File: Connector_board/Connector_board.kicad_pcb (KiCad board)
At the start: 2 copper layers, 54.2 x 20 mm, 7 parts, among them J1 SM03B-SRSS-TB, J2 USB_B_Micro, J3 Conn_02x07_Counter_Clockwise, J4 Conn_02x07_Odd_Even, J5 Conn_02x07_Counter_Clockwise

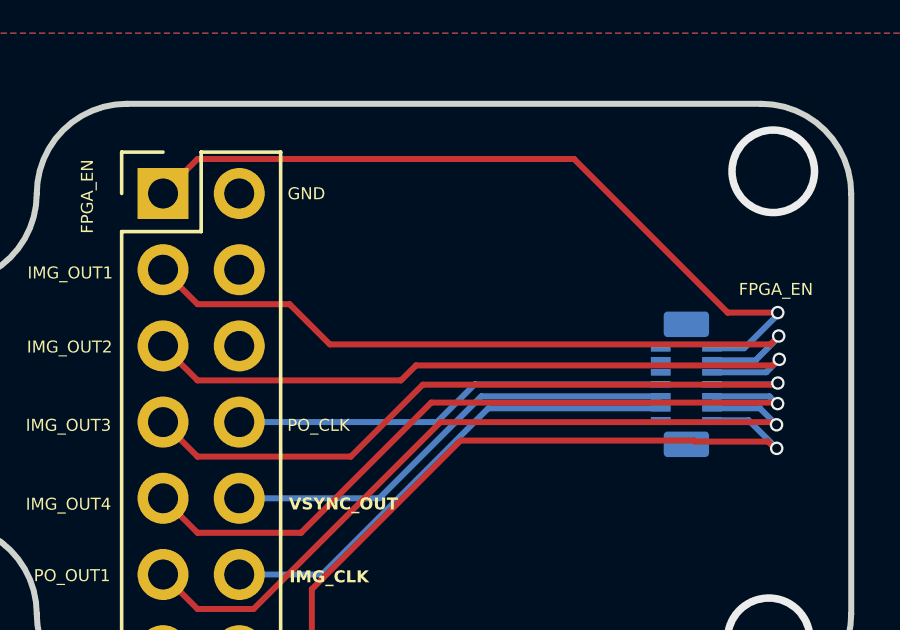
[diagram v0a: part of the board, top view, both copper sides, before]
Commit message: GPIO_1 added
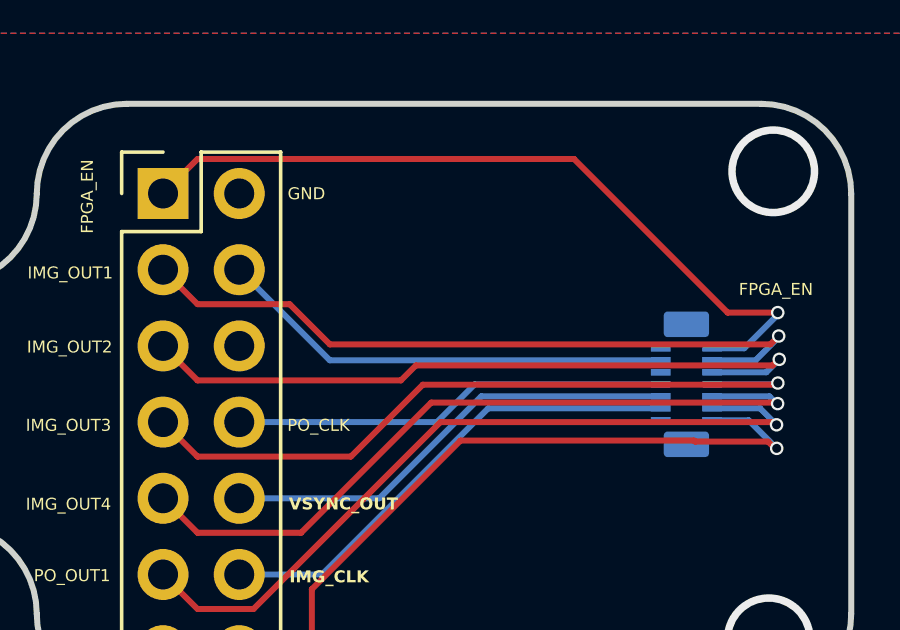
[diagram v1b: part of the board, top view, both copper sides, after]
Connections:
- J4 pad 11: /POSITION_OUT_1 -> /FPGA_CTRL
- J4 pad 4: unconnected-(J4-Pin_4-Pad4) -> /POSITION_OUT_1
- J5 pad 12: unconnected-(J5-Pin_12-Pad12) -> /POSITION_OUT_1
- J5 pad 3: /POSITION_OUT_1 -> /FPGA_CTRL
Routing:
- net /FPGA_CTRL: track 0.00 -> 25.9 mm, vias 0 -> 1
- net /POSITION_OUT_1: track 25.9 -> 15.3 mm, vias 1 -> 0
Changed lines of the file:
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@@
 			(layers "*.Cu" "*.Mask")
 			(remove_unused_layers no)
-			(net "unconnected-(J4-Pin_4-Pad4)")
+			(net "/POSITION_OUT_1")
 			(pinfunction "Pin_4_4")
-			(pintype "passive+no_connect")
+			(pintype "passive")
 		)
 		(pad "5" thru_hole circle
@@
 			(layers "*.Cu" "*.Mask")
 			(remove_unused_layers no)
-			(net "/POSITION_OUT_1")
+			(net "/FPGA_CTRL")
 			(pinfunction "Pin_11_11")
 			(pintype "passive")
@@
 			(size 0.22 0.66)
 			(layers "B.Cu" "B.Mask" "B.Paste")
-			(net "/POSITION_OUT_1")
+			(net "/FPGA_CTRL")
 			(pinfunction "Pin_3_3")
 			(pintype "passive")
@@
 			(size 0.22 0.66)
 			(layers "B.Cu" "B.Mask" "B.Paste")
-			(net "unconnected-(J5-Pin_12-Pad12)")
+			(net "/POSITION_OUT_1")
 			(pinfunction "Pin_12_12")
-			(pintype "passive+no_connect")
+			(pintype "passive")
 		)
 		(pad "13" smd rect
@@
 	)
 	(segment
-		(start 47.66 49.54)
-		(end 46.51 48.39)
-		(width 0.2)
-		(layer "F.Cu")
+		(start 52.07 41.25)
+		(end 49.05 38.23)
+		(width 0.2)
+		(layer "B.Cu")
 		(net "/POSITION_OUT_1")
 	)
 	(segment
-		(start 66.854856 43.31)
-		(end 55.756346 43.31)
-		(width 0.2)
-		(layer "F.Cu")
-		(net "/POSITION_OUT_1")
-	)
-	(segment
-		(start 55.756346 43.31)
-		(end 49.526346 49.54)
-		(width 0.2)
-		(layer "F.Cu")
-		(net "/POSITION_OUT_1")
-	)
-	(segment
-		(start 66.96 43.4)
-		(end 66.944856 43.4)
-		(width 0.2)
-		(layer "F.Cu")
-		(net "/POSITION_OUT_1")
-	)
-	(segment
-		(start 49.526346 49.54)
-		(end 47.66 49.54)
-		(width 0.2)
-		(layer "F.Cu")
-		(net "/POSITION_OUT_1")
-	)
-	(segment
-		(start 66.944856 43.4)
-		(end 66.854856 43.31)
-		(width 0.2)
-		(layer "F.Cu")
-		(net "/POSITION_OUT_1")
-	)
-	(via
-		(at 66.96 43.4)
-		(size 0.45)
-		(drill 0.3)
-		(layers "F.Cu" "B.Cu")
-		(net "/POSITION_OUT_1")
-	)
-	(segment
-		(start 66.41 42.85)
-		(end 64.81 42.85)
-		(width 0.2)
-		(layer "B.Cu")
-		(net "/POSITION_OUT_1")
-	)
-	(segment
-		(start 66.96 43.4)
-		(end 66.41 42.85)
+		(start 63.1 41.25)
+		(end 52.07 41.25)
 		(width 0.2)
 		(layer "B.Cu")
@@
 		(net "/USB_D1+")
 	)
+	(segment
+		(start 47.66 49.54)
+		(end 46.51 48.39)
+		(width 0.2)
+		(layer "F.Cu")
+		(net "/FPGA_CTRL")
+	)
+	(segment
+		(start 66.854856 43.31)
+		(end 55.756346 43.31)
+		(width 0.2)
+		(layer "F.Cu")
+		(net "/FPGA_CTRL")
+	)
+	(segment
+		(start 55.756346 43.31)
+		(end 49.526346 49.54)
+		(width 0.2)
+		(layer "F.Cu")
+		(net "/FPGA_CTRL")
+	)
+	(segment
+		(start 66.96 43.4)
+		(end 66.944856 43.4)
+		(width 0.2)
+		(layer "F.Cu")
+		(net "/FPGA_CTRL")
+	)
+	(segment
+		(start 49.526346 49.54)
+		(end 47.66 49.54)
+		(width 0.2)
+		(layer "F.Cu")
+		(net "/FPGA_CTRL")
+	)
+	(segment
+		(start 66.944856 43.4)
+		(end 66.854856 43.31)
+		(width 0.2)
+		(layer "F.Cu")
+		(net "/FPGA_CTRL")
+	)
+	(via
+		(at 66.96 43.4)
+		(size 0.45)
+		(drill 0.3)
+		(layers "F.Cu" "B.Cu")
+		(net "/FPGA_CTRL")
+	)
+	(segment
+		(start 66.41 42.85)
+		(end 64.81 42.85)
+		(width 0.2)
+		(layer "B.Cu")
+		(net "/FPGA_CTRL")
+	)
+	(segment
+		(start 66.96 43.4)
+		(end 66.41 42.85)
+		(width 0.2)
+		(layer "B.Cu")
+		(net "/FPGA_CTRL")
+	)
 	(zone

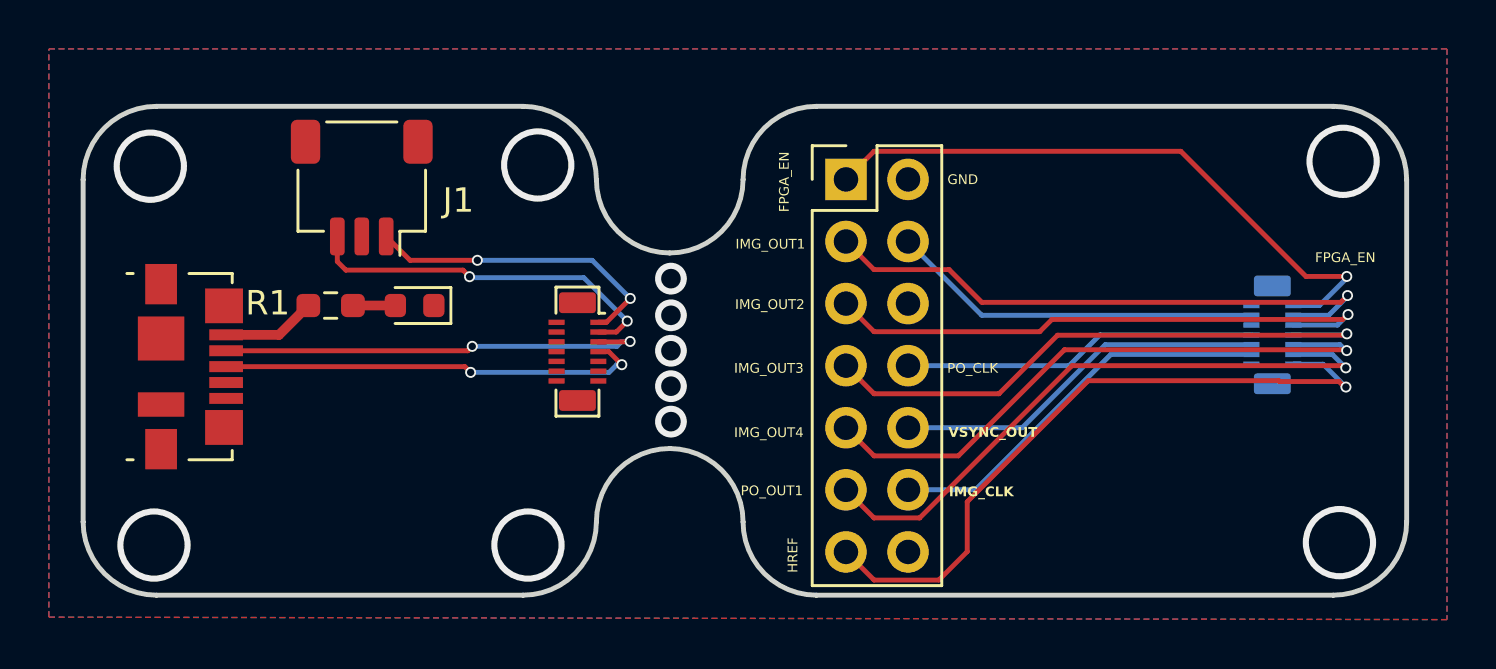
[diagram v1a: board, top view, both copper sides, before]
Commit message: connector board pin order updated
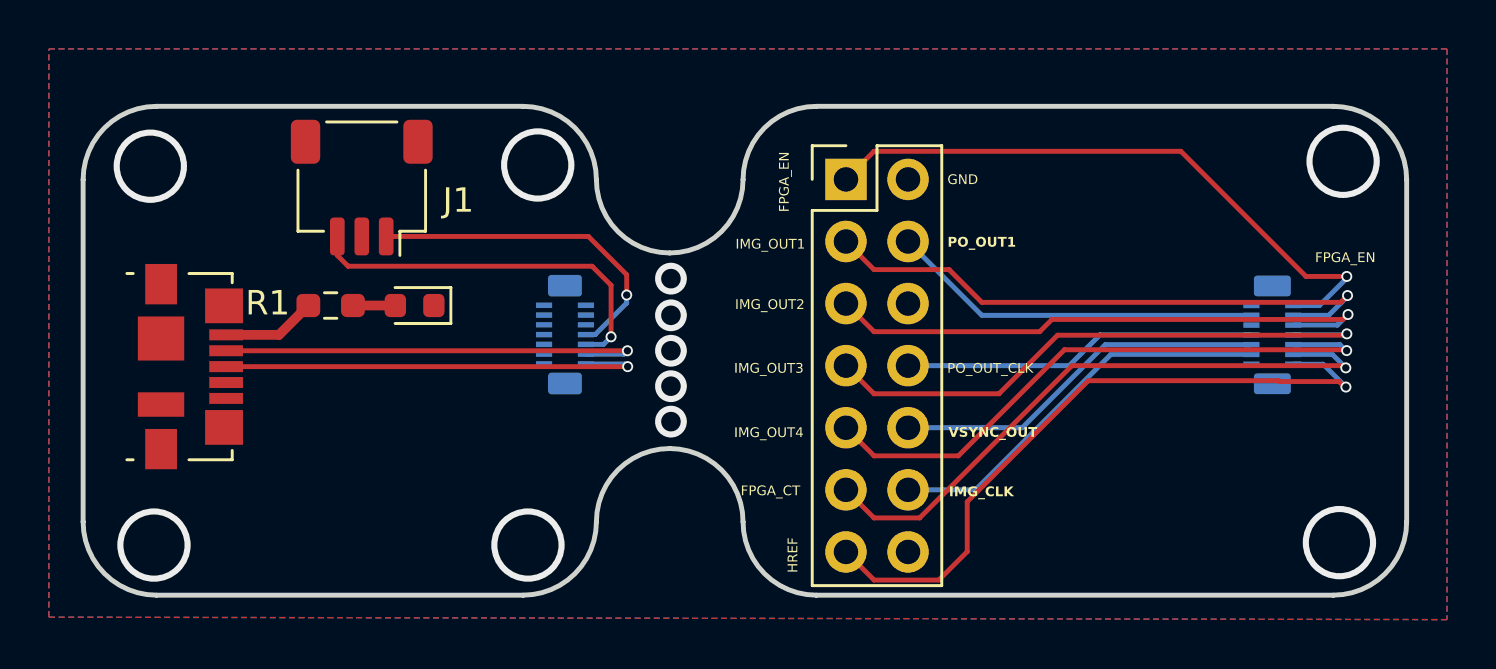
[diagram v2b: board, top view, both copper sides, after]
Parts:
- J3: moved to B.Cu
- moved J3 0.86 mm to (35.0, 42.0), turned to 90 degrees
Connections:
- J3 pad 1: /SWD_1 -> /USB_D1+
- J3 pad 3: /SWCLK_1 -> /USB_D1-
- J3 pad 5: /USB_D1- -> /SWCLK_1
- J3 pad 7: /USB_D1+ -> /SWD_1
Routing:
- net /SWD_1: track 13.2 -> 14.3 mm, vias 2 -> 1
- net /USB_D1+: track 17.6 -> 18.2 mm, vias 2 -> 1
- net /SWCLK_1: track 15.2 -> 15.7 mm, vias 2 -> 1
- net /USB_D1-: track 18.0 -> 18.2 mm, vias 2 -> 1
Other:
- board text added: "FPGA_CT"
- board text added: "PO_OUT_CLK"
- board text removed: "PO_CLK"

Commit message: new connector footprint updated
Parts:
- removed J4: Conn_02x07_Odd_Even, Connector_PinHeader_2.54mm:PinHeader_2x07_P2.54mm_Vertical
- added J6: Conn_02x06_Top_Bottom, 5035521222:CON_5035521222, B.Cu at (34.8, 42.2)
- J3: value Conn_02x07_Counter_Clockwise -> Conn_02x06_Odd_Even; footprint Connector_Molex:Molex_SlimStack_502430-1410_2x07_P0.40mm_Vertical -> Connector_PinHeader_2.54mm:PinHeader_2x06_P2.54mm_Vertical; moved to F.Cu
- J5: value Conn_02x07_Counter_Clockwise -> Conn_02x06_Top_Bottom; footprint Connector_Molex:Molex_SlimStack_502430-1410_2x07_P0.40mm_Vertical -> 5035521222:CON_5035521222
- moved J3 14.0 mm to (47.9, 36.5), turned to 0 degrees
- moved J5 0.91 mm to (64.2, 42.9)
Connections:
- J3 pad 1: /USB_D1+ -> GND
- J3 pad 10: unconnected-(J3-Pin_10-Pad10) -> /IMAGE_OUT_4
- J3 pad 11: unconnected-(J3-Pin_11-Pad11) -> /HREF_OUT
- J3 pad 12: unconnected-(J3-Pin_12-Pad12) -> /FPGA_CTRL
- J3 pad 2: unconnected-(J3-Pin_2-Pad2) -> /FPGA_EN
- J3 pad 3: /USB_D1- -> /POSITION_OUT_1
- J3 pad 4: unconnected-(J3-Pin_4-Pad4) -> /IMAGE_OUT_1
- J3 pad 5: /SWCLK_1 -> /POSITION_OUT_CLK
- J3 pad 6: unconnected-(J3-Pin_6-Pad6) -> /IMAGE_OUT_2
- J3 pad 7: /SWD_1 -> /VSYNC_OUT
- J3 pad 8: unconnected-(J3-Pin_8-Pad8) -> /IMAGE_OUT_3
- J3 pad 9: unconnected-(J3-Pin_9-Pad9) -> /IMAGE_CLK
- J5 pad 1: /HREF_OUT -> /FPGA_CTRL
- J5 pad 10: unconnected-(J5-Pin_10-Pad10) -> /POSITION_OUT_CLK
- J5 pad 11: /IMAGE_OUT_1 -> /POSITION_OUT_1
- J5 pad 12: /POSITION_OUT_1 -> GND
- J5 pad 2: unconnected-(J5-Pin_2-Pad2) -> /IMAGE_OUT_4
- J5 pad 3: /FPGA_CTRL -> /IMAGE_OUT_3
- J5 pad 4: /IMAGE_CLK -> /IMAGE_OUT_2
- J5 pad 5: /IMAGE_OUT_4 -> /IMAGE_OUT_1
- J5 pad 6: /VSYNC_OUT -> /FPGA_EN
- J5 pad 7: /IMAGE_OUT_3 -> /HREF_OUT
- J5 pad 8: /POSITION_OUT_CLK -> /IMAGE_CLK
- J5 pad 9: /IMAGE_OUT_2 -> /VSYNC_OUT
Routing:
- net /HREF_OUT: track 28.2 -> 18.4 mm, vias 1 -> 0
- net /FPGA_EN: track 25.8 -> 21.5 mm
- net /IMAGE_OUT_3: track 24.2 -> 20.4 mm
- net /FPGA_CTRL: track 25.9 -> 22.2 mm
- net /IMAGE_OUT_4: track 24.9 -> 21.3 mm
- net /IMAGE_OUT_2: track 23.7 -> 20.5 mm
- net GND: track 0.00 -> 3.04 mm, vias 11 -> 13
- net /IMAGE_OUT_1: track 24.2 -> 21.4 mm
- net /POSITION_OUT_1: track 15.3 -> 16.6 mm
- net /VSYNC_OUT: track 15.5 -> 16.6 mm
- net /IMAGE_CLK: track 16.3 -> 17.5 mm
- net /POSITION_OUT_CLK: track 14.6 -> 15.7 mm
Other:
- board text added: "FPGA_CTRL"
- board text added: "HREF_OUT"
- board text added: "PO_OUT_1"
- board text removed: "FPGA_CT"
- board text removed: "HREF"
- board text removed: "PO_OUT1"

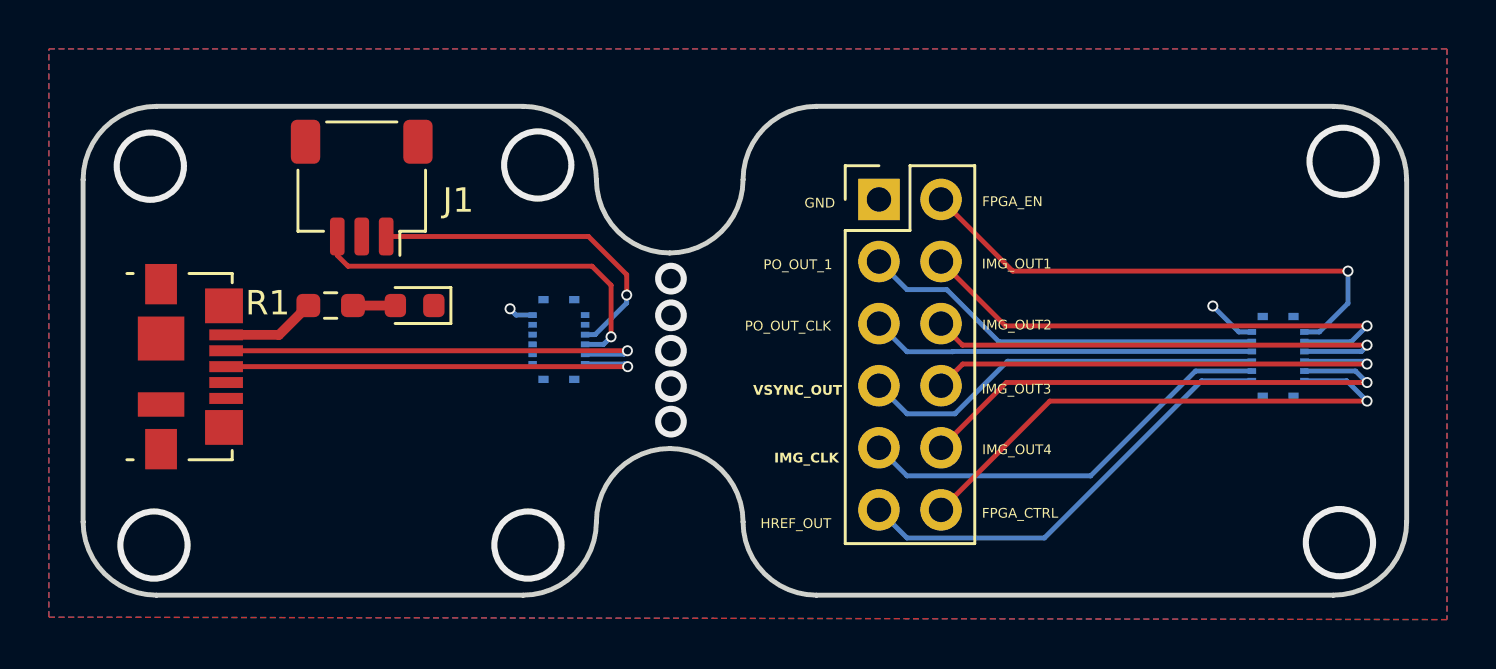
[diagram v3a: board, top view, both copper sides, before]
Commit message: connector footprint swapped
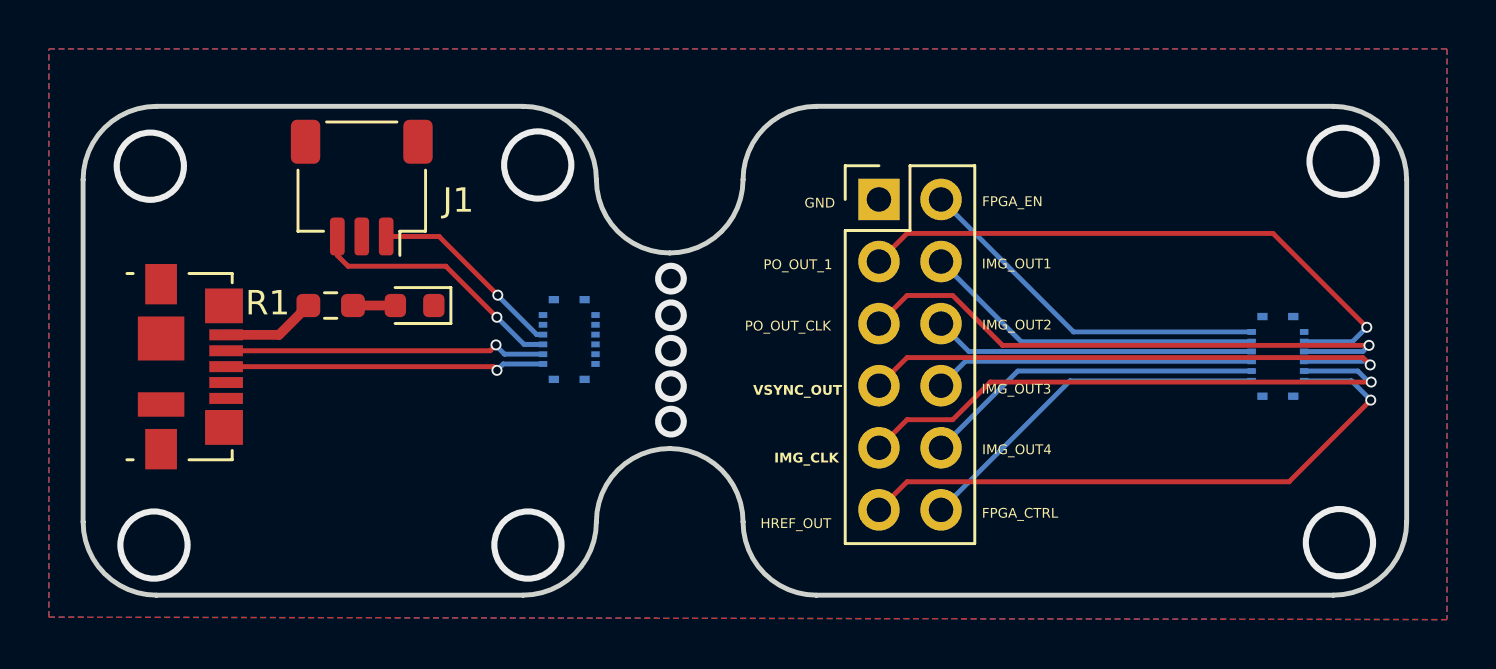
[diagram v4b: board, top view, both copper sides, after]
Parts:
- moved J6 0.42 mm to (35.2, 42.2)
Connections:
- J5 pad 1: /FPGA_CTRL -> /HREF_OUT
- J5 pad 10: /POSITION_OUT_CLK -> /IMAGE_OUT_2
- J5 pad 11: /POSITION_OUT_1 -> /IMAGE_OUT_1
- J5 pad 12: GND -> /FPGA_EN
- J5 pad 2: /IMAGE_OUT_4 -> /IMAGE_CLK
- J5 pad 3: /IMAGE_OUT_3 -> /VSYNC_OUT
- J5 pad 4: /IMAGE_OUT_2 -> /POSITION_OUT_CLK
- J5 pad 5: /IMAGE_OUT_1 -> /POSITION_OUT_1
- J5 pad 6: /FPGA_EN -> GND
- J5 pad 7: /HREF_OUT -> /FPGA_CTRL
- J5 pad 8: /IMAGE_CLK -> /IMAGE_OUT_4
- J5 pad 9: /VSYNC_OUT -> /IMAGE_OUT_3
- J6 pad 1: /USB_D1+ -> unconnected-(J6-Pin_1-Pad1)
- J6 pad 10: unconnected-(J6-Pin_10-Pad10) -> /SWD_1
- J6 pad 12: GND -> unconnected-(J6-Pin_12-Pad12)
- J6 pad 2: /USB_D1- -> unconnected-(J6-Pin_2-Pad2)
- J6 pad 3: /SWCLK_1 -> unconnected-(J6-Pin_3-Pad3)
- J6 pad 4: /SWD_1 -> unconnected-(J6-Pin_4-Pad4)
- J6 pad 6: unconnected-(J6-Pin_6-Pad6) -> GND
- J6 pad 7: unconnected-(J6-Pin_7-Pad7) -> /USB_D1+
- J6 pad 8: unconnected-(J6-Pin_8-Pad8) -> /USB_D1-
- J6 pad 9: unconnected-(J6-Pin_9-Pad9) -> /SWCLK_1
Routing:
- net /POSITION_OUT_CLK: track 15.7 -> 24.1 mm, vias 0 -> 1
- net /POSITION_OUT_1: track 16.6 -> 24.8 mm, vias 0 -> 1
- net /IMAGE_OUT_2: track 20.5 -> 13.2 mm, vias 1 -> 0
- net /FPGA_CTRL: track 22.2 -> 14.9 mm, vias 1 -> 0
- net /IMAGE_OUT_4: track 21.3 -> 14.0 mm, vias 1 -> 0
- net /IMAGE_OUT_3: track 20.4 -> 13.1 mm, vias 1 -> 0
- net /IMAGE_OUT_1: track 21.4 -> 14.1 mm, vias 1 -> 0
- net /VSYNC_OUT: track 16.6 -> 23.4 mm, vias 0 -> 1
- net /IMAGE_CLK: track 17.5 -> 24.2 mm, vias 0 -> 1
- net /HREF_OUT: track 18.4 -> 25.0 mm, vias 0 -> 1
- net /FPGA_EN: track 21.5 -> 15.0 mm, vias 1 -> 0
- net /SWD_1: track 14.3 -> 8.54 mm
- net /SWCLK_1: track 15.7 -> 10.7 mm
- net /USB_D1+: track 18.2 -> 13.1 mm
- net /USB_D1-: track 18.2 -> 13.2 mm
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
